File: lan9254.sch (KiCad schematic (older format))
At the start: 31 parts, among them U1 lan9254, X1 FNETHE025

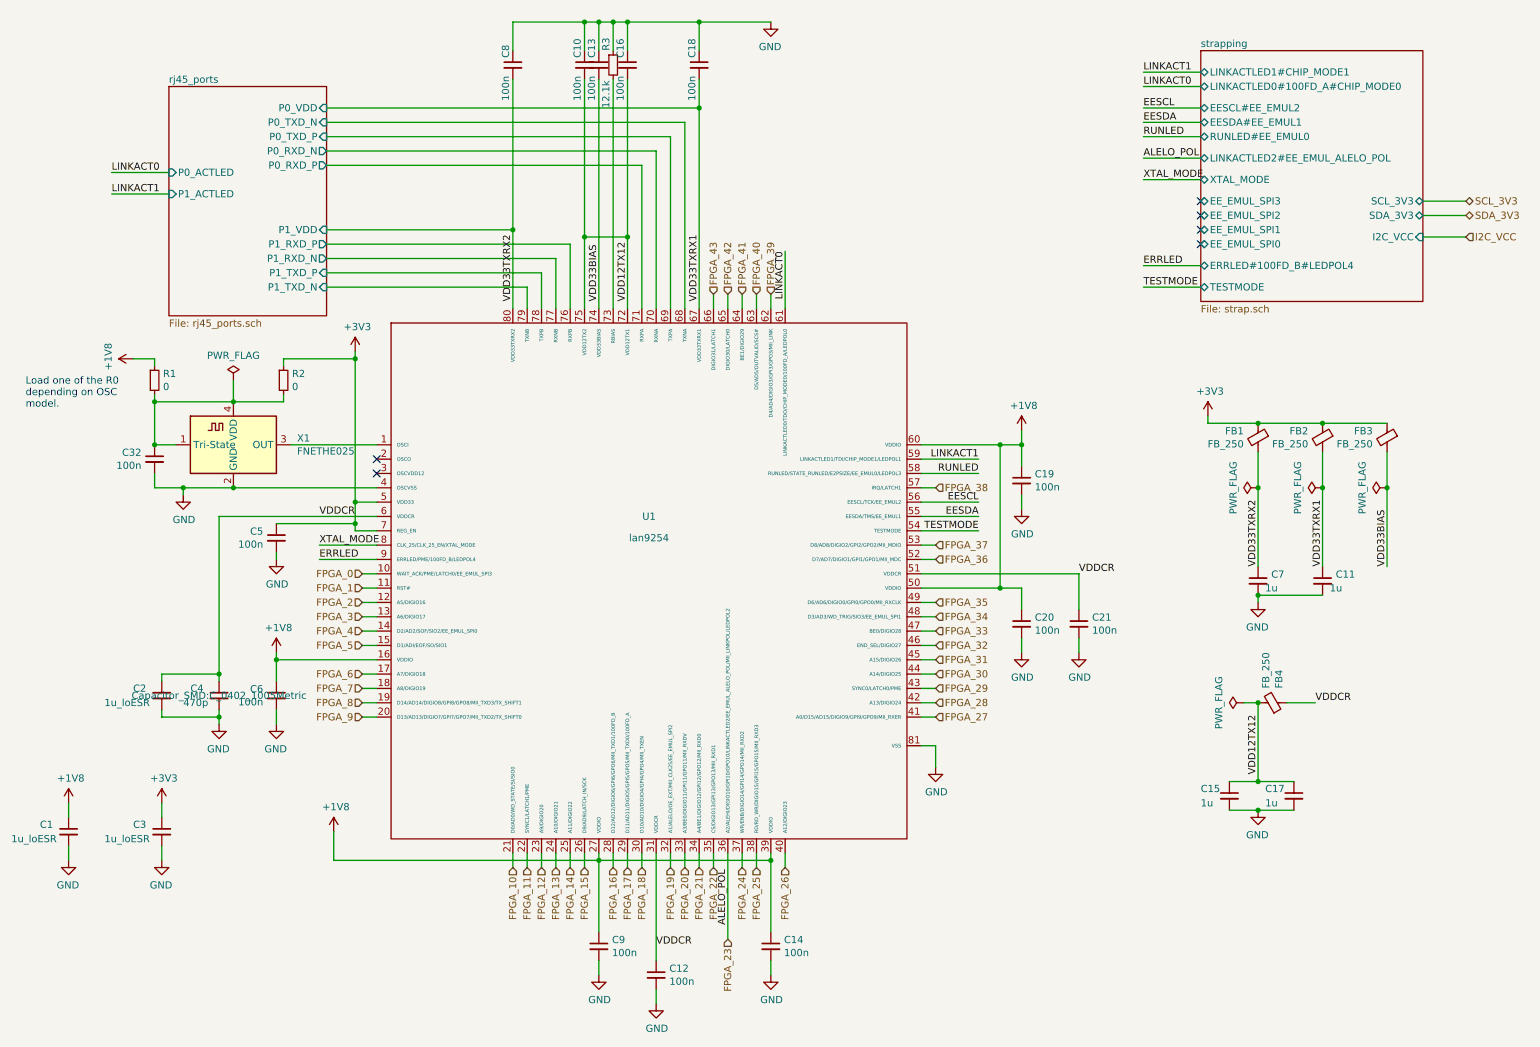
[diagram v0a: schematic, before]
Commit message: added I/O connectors, JTAG (just in case) and more
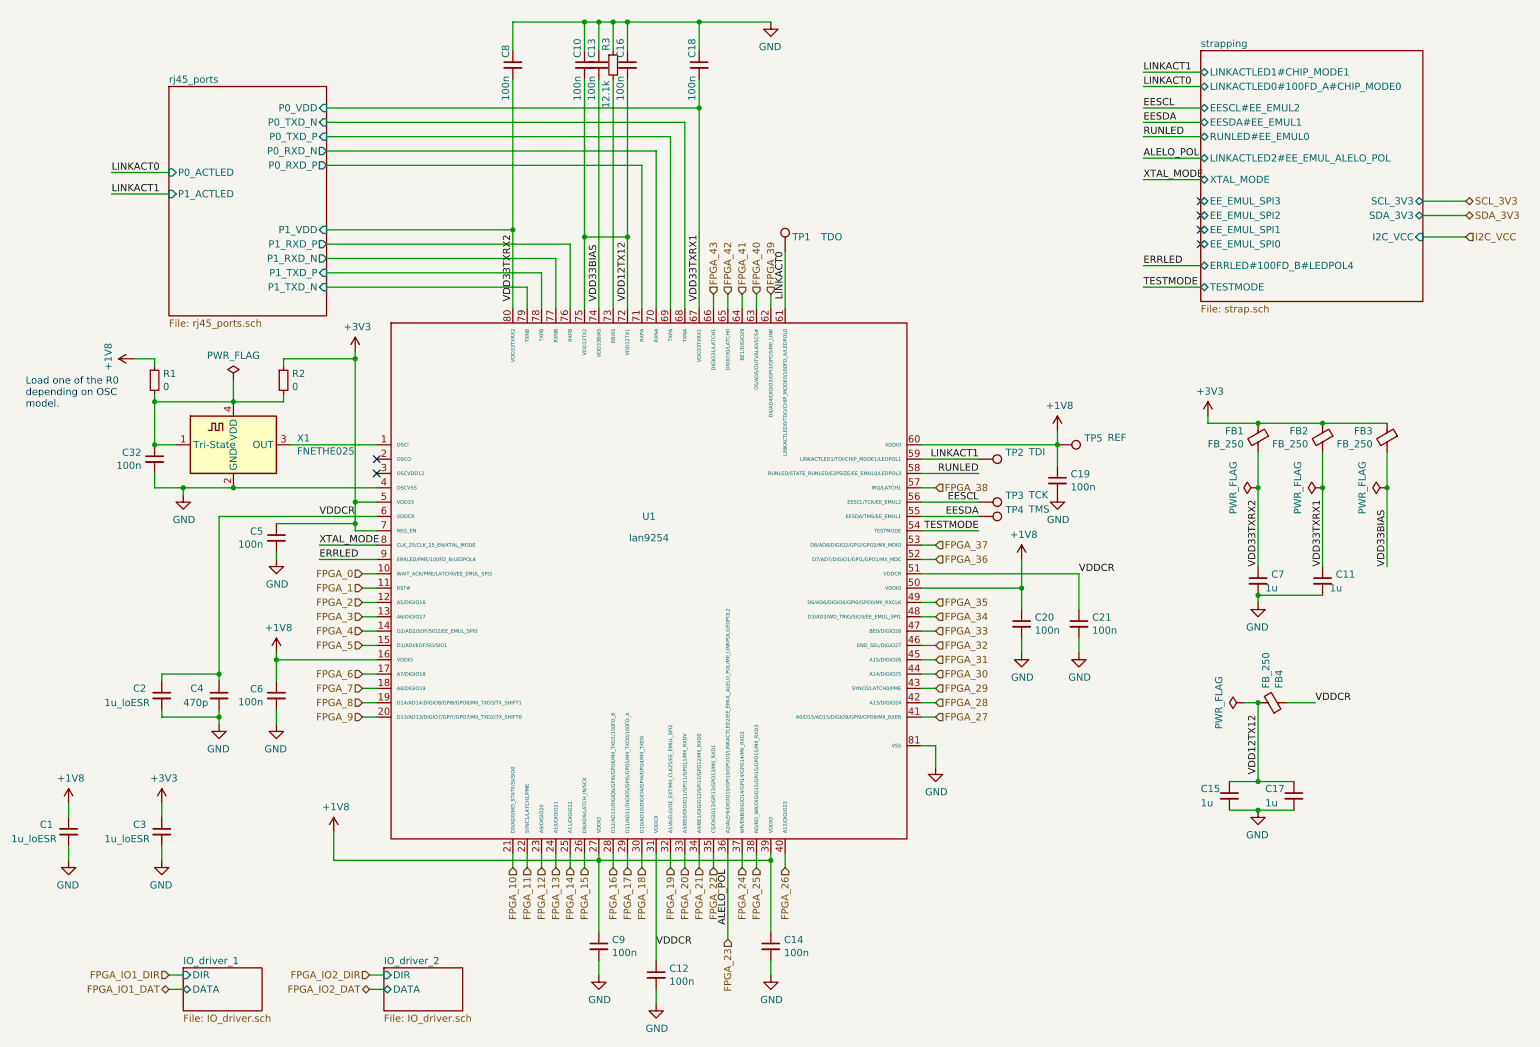
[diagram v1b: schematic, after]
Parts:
- added TP1: TDO, Connector_PinHeader_1.27mm:PinHeader_1x01_P1.27mm_Vertical, symbol Connector:TestPoint
- added TP2: TDI, Connector_PinHeader_1.27mm:PinHeader_1x01_P1.27mm_Vertical, symbol Connector:TestPoint
- added TP3: TCK, Connector_PinHeader_1.27mm:PinHeader_1x01_P1.27mm_Vertical, symbol Connector:TestPoint
- added TP4: TMS, Connector_PinHeader_1.27mm:PinHeader_1x01_P1.27mm_Vertical, symbol Connector:TestPoint
- added TP5: REF, Connector_PinHeader_1.27mm:PinHeader_1x01_P1.27mm_Vertical, symbol Connector:TestPoint
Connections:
- net +1V8_lan9254: now also TP5.1
- net EESCL: now also TP3.1
- net EESDA: now also TP4.1
- net LINKACT0: now also TP1.1
- net LINKACT1: now also TP2.1
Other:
- moved on the sheet: C19
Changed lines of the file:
@@
 $Descr A4 11693 8268
 encoding utf-8
-Sheet 2 4
+Sheet 2 6
 Title ""
 Date ""
@@
 	8050 4900 8050 5000
 Wire Wire Line
-	6950 4550 7500 4550
-Wire Wire Line
 	7650 4550 7650 4700
 Wire Wire Line
@@
 L Device:C_Small C19
 U 1 1 60E78D0A
-P 7650 3800
-F 0 "C19" H 7742 3846 50  0000 L CNN
-F 1 "100n" H 7742 3755 50  0000 L CNN
-F 2 "Capacitor_SMD:C_0402_1005Metric" H 7650 3800 50  0001 C CNN
-F 3 "~" H 7650 3800 50  0001 C CNN
-	1    7650 3800
+P 7900 3800
+F 0 "C19" H 7992 3846 50  0000 L CNN
+F 1 "100n" H 7992 3755 50  0000 L CNN
+F 2 "Capacitor_SMD:C_0402_1005Metric" H 7900 3800 50  0001 C CNN
+F 3 "~" H 7900 3800 50  0001 C CNN
+	1    7900 3800
 	1    0    0    -1
 $EndComp
@@
 L lan9254_project:GND #PWR?
 U 1 1 60E78EE6
-P 7650 4000
+P 7900 3900
 AR Path="/60DC28BD/60E78EE6" Ref="#PWR?"  Part="1"
 AR Path="/60E78EE6" Ref="#PWR?"  Part="1"
 AR Path="/60DB2574/60E78EE6" Ref="#PWR?"  Part="1"
-F 0 "#PWR?" H 7650 3750 50  0001 C CNN
-F 1 "GND" H 7655 3827 50  0000 C CNN
-F 2 "" H 7650 4000 50  0001 C CNN
-F 3 "" H 7650 4000 50  0001 C CNN
-	1    7650 4000
-	1    0    0    -1
-$EndComp
-Wire Wire Line
-	7650 3900 7650 4000
-Wire Wire Line
-	6950 3550 7500 3550
-Wire Wire Line
-	7650 3550 7650 3700
+F 0 "#PWR?" H 7900 3650 50  0001 C CNN
+F 1 "GND" H 7905 3727 50  0000 C CNN
+F 2 "" H 7900 3900 50  0001 C CNN
+F 3 "" H 7900 3900 50  0001 C CNN
+	1    7900 3900
+	1    0    0    -1
+$EndComp
+Wire Wire Line
+	7900 3550 7900 3700
 $Comp
 L Device:C_Small C6
@@
 L lan9254_project:+1V8 #PWR?
 U 1 1 60E92892
-P 7650 3450
+P 7900 3450
 AR Path="/60DC28BD/60E92892" Ref="#PWR?"  Part="1"
 AR Path="/60E92892" Ref="#PWR?"  Part="1"
 AR Path="/60DB2574/60E92892" Ref="#PWR?"  Part="1"
-F 0 "#PWR?" H 7650 3300 50  0001 C CNN
-F 1 "+1V8" H 7665 3623 50  0000 C CNN
-F 2 "" H 7650 3450 50  0001 C CNN
-F 3 "" H 7650 3450 50  0001 C CNN
-	1    7650 3450
-	1    0    0    -1
-$EndComp
-Wire Wire Line
-	7650 3450 7650 3550
-Connection ~ 7650 3550
-Wire Wire Line
-	7500 3550 7500 4550
-Connection ~ 7500 3550
-Wire Wire Line
-	7500 3550 7650 3550
-Connection ~ 7500 4550
-Wire Wire Line
-	7500 4550 7650 4550
+F 0 "#PWR?" H 7900 3300 50  0001 C CNN
+F 1 "+1V8" H 7915 3623 50  0000 C CNN
+F 2 "" H 7900 3450 50  0001 C CNN
+F 3 "" H 7900 3450 50  0001 C CNN
+	1    7900 3450
+	1    0    0    -1
+$EndComp
+Wire Wire Line
+	7900 3450 7900 3550
+Connection ~ 7900 3550
 $Comp
 L Device:C_Small C5
@@
 F 0 "C4" H 1850 5350 50  0000 L CNN
 F 1 "470p" H 1800 5250 50  0000 L CNN
-F 2 "Capacitor_SMD:C_0402_1005Metric" H 2050 5300 50  0000 C CNN
+F 2 "Capacitor_SMD:C_0402_1005Metric" H 2050 5300 50  0001 C CNN
 F 3 "~" H 2050 5300 50  0001 C CNN
 	1    2050 5300
@@
 	1600 3850 1800 3850
 Connection ~ 1800 3850
+$Sheet
+S 1800 7200 550  300
+U 60EF9F81
+F0 "IO_driver_1" 50
+F1 "IO_driver.sch" 50
+F2 "DATA" B L 1800 7350 50
+F3 "DIR" I L 1800 7250 50
+$EndSheet
+$Sheet
+S 3200 7200 550  300
+U 60E556C7
+F0 "IO_driver_2" 50
+F1 "IO_driver.sch" 50
+F2 "DATA" B L 3200 7350 50
+F3 "DIR" I L 3200 7250 50
+$EndSheet
+Text HLabel 3100 7250 0    50   Input ~ 0
+FPGA_IO2_DIR
+Text HLabel 3100 7350 0    50   BiDi ~ 0
+FPGA_IO2_DAT
+Text HLabel 1700 7350 0    50   BiDi ~ 0
+FPGA_IO1_DAT
+Text HLabel 1700 7250 0    50   Input ~ 0
+FPGA_IO1_DIR
+Wire Wire Line
+	1700 7350 1800 7350
+Wire Wire Line
+	1700 7250 1800 7250
+Wire Wire Line
+	3100 7250 3200 7250
+Wire Wire Line
+	3100 7350 3200 7350
+$Comp
+L Connector:TestPoint TP1
+U 1 1 60E57CD1
+P 6000 2200
+F 0 "TP1" H 6050 2300 50  0000 L CNN
+F 1 "TDO" H 6250 2300 50  0000 L CNN
+F 2 "Connector_PinHeader_1.27mm:PinHeader_1x01_P1.27mm_Vertical" H 6200 2200 50  0001 C CNN
+F 3 "~" H 6200 2200 50  0001 C CNN
+	1    6000 2200
+	1    0    0    -1
+$EndComp
+$Comp
+L Connector:TestPoint TP2
+U 1 1 60E58942
+P 7350 3650
+F 0 "TP2" V 7304 3838 50  0000 L CNN
+F 1 "TDI" V 7300 4000 50  0000 L CNN
+F 2 "Connector_PinHeader_1.27mm:PinHeader_1x01_P1.27mm_Vertical" H 7550 3650 50  0001 C CNN
+F 3 "~" H 7550 3650 50  0001 C CNN
+	1    7350 3650
+	0    1    1    0
+$EndComp
+Wire Wire Line
+	6950 4550 7650 4550
+$Comp
+L lan9254_project:+1V8 #PWR?
+U 1 1 60E5950A
+P 7650 4350
+AR Path="/60DC28BD/60E5950A" Ref="#PWR?"  Part="1"
+AR Path="/60E5950A" Ref="#PWR?"  Part="1"
+AR Path="/60DB2574/60E5950A" Ref="#PWR?"  Part="1"
+F 0 "#PWR?" H 7650 4200 50  0001 C CNN
+F 1 "+1V8" H 7665 4523 50  0000 C CNN
+F 2 "" H 7650 4350 50  0001 C CNN
+F 3 "" H 7650 4350 50  0001 C CNN
+	1    7650 4350
+	1    0    0    -1
+$EndComp
+Wire Wire Line
+	7650 4550 7650 4350
+Connection ~ 7650 4550
+Wire Wire Line
+	6950 3550 7900 3550
+$Comp
+L Connector:TestPoint TP3
+U 1 1 60E83DE3
+P 7350 3950
+F 0 "TP3" V 7304 4138 50  0000 L CNN
+F 1 "TCK" V 7300 4300 50  0000 L CNN
+F 2 "Connector_PinHeader_1.27mm:PinHeader_1x01_P1.27mm_Vertical" H 7550 3950 50  0001 C CNN
+F 3 "~" H 7550 3950 50  0001 C CNN
+	1    7350 3950
+	0    1    1    0
+$EndComp
+$Comp
+L Connector:TestPoint TP4
+U 1 1 60E841F7
+P 7350 4050
+F 0 "TP4" V 7304 4238 50  0000 L CNN
+F 1 "TMS" V 7300 4400 50  0000 L CNN
+F 2 "Connector_PinHeader_1.27mm:PinHeader_1x01_P1.27mm_Vertical" H 7550 4050 50  0001 C CNN
+F 3 "~" H 7550 4050 50  0001 C CNN
+	1    7350 4050
+	0    1    1    0
+$EndComp
+$Comp
+L Connector:TestPoint TP5
+U 1 1 60E8477A
+P 7900 3550
+F 0 "TP5" V 7854 3738 50  0000 L CNN
+F 1 "REF" V 7850 3900 50  0000 L CNN
+F 2 "Connector_PinHeader_1.27mm:PinHeader_1x01_P1.27mm_Vertical" H 8100 3550 50  0001 C CNN
+F 3 "~" H 8100 3550 50  0001 C CNN
+	1    7900 3550
+	0    1    1    0
+$EndComp
 $EndSCHEMATC

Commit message: reannotated for merging with te0715 development board
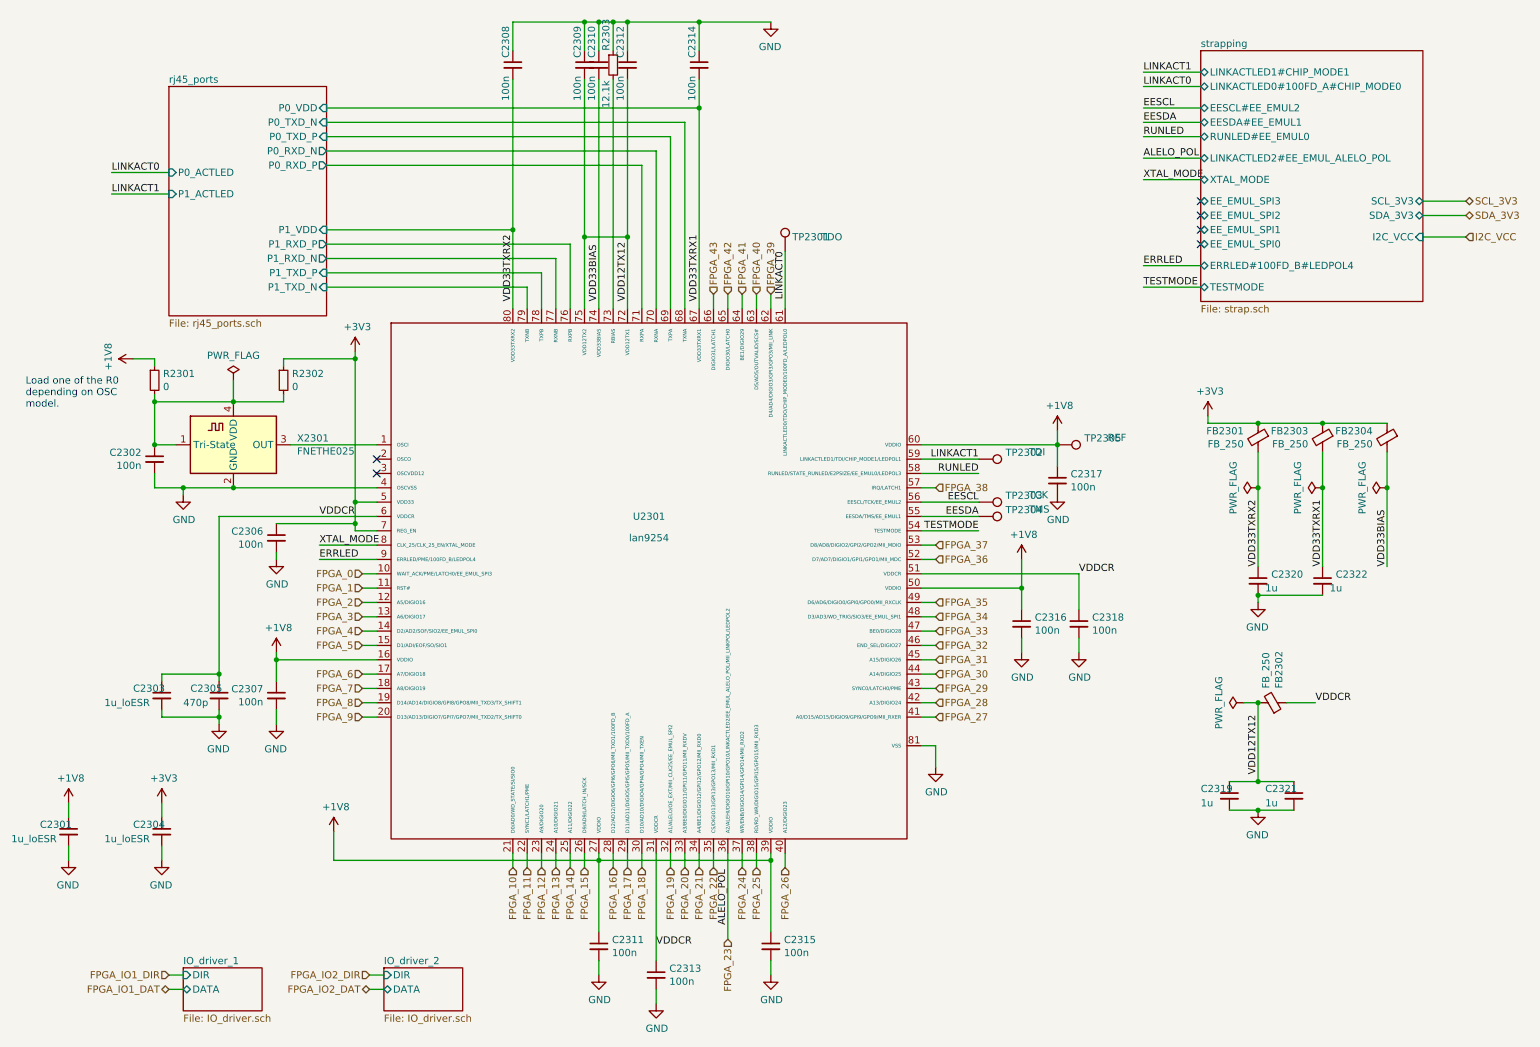
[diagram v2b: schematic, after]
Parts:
- renumbered C1 to C2301, C32 to C2302, C2 to C2303, C3 to C2304, C4 to C2305, C5 to C2306, C6 to C2307, C8 to C2308, C10 to C2309, C13 to C2310, C9 to C2311, C16 to C2312, C12 to C2313, C18 to C2314, C14 to C2315, C20 to C2316, C19 to C2317, C21 to C2318, C15 to C2319, C7 to C2320, C17 to C2321, C11 to C2322, FB1 to FB2301, FB2 to FB2303, FB3 to FB2304, TP1 to TP2301, TP2 to TP2302, TP3 to TP2303, TP4 to TP2304, TP5 to TP2305, U1 to U2301, X1 to X2301
